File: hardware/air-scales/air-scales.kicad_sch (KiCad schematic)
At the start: 52 parts, among them J1 Connector, USB-TYPE-C-16P, Q1 C458246, SW1 B3FS-1000, SW2 B3FS-1000, U1 BME280, U2 TPS62162DSG, U3 SMA6T28AY, U4 SMA6T15AY, U5 LM74610QDGKTQ1, U6 LM63625DQPWPRQ1, U7 TPS2553DRVR, U8 TPS2121RUXR, U9 ESP32-S3-WROOM-1U-N16R8

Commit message: fixed some schematic bullshit i think, still need tvs on vbus
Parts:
- added C21: 10nF, PCM_JLCPCB:C_0603, symbol PCM_JLCPCB-Capacitors:0603,10nF
- added C22, C23: 100nF, PCM_JLCPCB:C_0603, symbol PCM_JLCPCB-Capacitors:0603,100nF
- added C24, C25, C26: 10uF, PCM_JLCPCB:C_1206, symbol PCM_JLCPCB-Capacitors:1206,10uF
- added D4: ESD5Z5.0, Diode_SMD:D_SOD-523, symbol Diode:ESD5Zxx
- added D5: Red, PCM_JLCPCB:D_0603, symbol PCM_JLCPCB-Diodes:LED,0603,Red
- added D7: YELLOW, PCM_JLCPCB:D_0603, symbol PCM_JLCPCB-Diodes:LED,0603,Red
- added D8: ORANGE, PCM_JLCPCB:D_0603, symbol PCM_JLCPCB-Diodes:LED,0603,Red
- added D9: WS2812B, PCM_JLCPCB:LED-SMD_4P-L1.6-W1.5_XL-1615RGBC-WS2812B, symbol PCM_JLCPCB-Extended:LED, WS2812B, 1615
- added J2, J5: Conn_01x03_Socket, symbol Connector:Conn_01x03_Socket
- added J3: Conn_01x02_Socket, symbol Connector:Conn_01x02_Socket
- added R14, R17, R18: 4.7kΩ, PCM_JLCPCB:R_0603, symbol PCM_JLCPCB-Resistors:0603,4.7kΩ
- added R15, R16: 10kΩ, PCM_JLCPCB:R_0603, symbol PCM_JLCPCB-Resistors:0603,10kΩ
- added R19: 470Ω, PCM_JLCPCB:R_0603, symbol PCM_JLCPCB-Resistors:0603,3.3kΩ
- added R20: 1kΩ, PCM_JLCPCB:R_0603, symbol PCM_JLCPCB-Resistors:0603,3.3kΩ
- C13: Capacitance 120uF -> 10uF; LCSC (none) -> C96446; Price (none) -> 0.021USD; Stock (none) -> 3388297
- C2: Attrition Qty (none) -> 10; Category (none) -> Capacitors,Multilayer Ceramic Capacitors MLCC - SMD/SMT; Class (none) -> Basic Component; LCSC C531423 -> C1546; Manufacturer TDK -> FH(Guangdong Fenghua Advanced Tech); Minimum Qty (none) -> 20; Part CGA2B2C0G2A101JT0Y0F -> 0402CG101J500NT; Price (none) -> 0.004USD; Process (none) -> SMT; Stock (none) -> 2554383; Voltage Rated 100V -> 50V
- C4: LCSC C472849 -> C50254; Price (none) -> 0.032USD; Stock (none) -> 180873
- C5: footprint LM74610:CAP_PC_10X12P7_NCH-M -> CAP_PC_10X12P7_NCH
- C7: Attrition Qty (none) -> 10; LCSC (none) -> C21120; Minimum Qty (none) -> 20; Part (none) -> CL10B224KA8NNNC; Stock (none) -> 781839; Voltage Rated 50V -> 25V
- D1, D2: Attrition Qty (none) -> 4; LCSC C20345394 -> C42413899; Manufacturer TI -> hongjiacheng; Minimum Qty (none) -> 5; Part ESD321DYAR -> H5VND5BA; Price (none) -> 0.032USD; Stock (none) -> 10812
- D3: Attrition Qty (none) -> 4; Class (none) -> Preferred Component; LCSC C22427765 -> C41411782; Manufacturer TI -> hongjiacheng; Minimum Qty (none) -> 15; Part ESD441DPLR -> SMF20A; Price (none) -> 0.026USD; Process (none) -> SMT; Stock (none) -> 34292
- D6: value Red -> GREEN
- L1: footprint Inductor_SMD:L_Coilcraft_1515SQ-68N -> PCM_JLCPCB:L_0805; Attrition Qty (none) -> 10; Class (none) -> Preferred Component; Frequency - Self Resonant (none) -> 50MHz; LCSC C404494 -> C1043; Manufacturer TDK -> FH(Guangdong Fenghua Advanced Tech); Minimum Qty (none) -> 20; Part VLS3012HBX-2R2M -> CMI201209U2R2KT; Price (none) -> 0.011USD; Process SMD -> SMT; Q @ Freq (none) -> 35@10MHz; Stock (none) -> 114084
- R3: value 3.3kΩ -> 1kΩ; Attrition Qty 10 -> (none); LCSC C22978 -> (none); Minimum Qty 20 -> (none); Price 0.004USD -> (none); Process SMT -> (none); Resistance 3.3kΩ -> 1kΩ; Stock 2152628 -> (none)
- U3, U4: footprint SMA6T28AY:SMA_UNI_STM -> SMA_UNI_STM
- U5: footprint LM74610:DGK0008A_N -> LM74610QDGKTQ1:SOP65P490X110-8N
- U9: footprint ESP32:XCVR_ESP32-S3-WROOM-1U-N16R8 -> ESP32-S3-WROOM-1U-N16R8:XCVR_ESP32-S3-WROOM-1U-N16R8
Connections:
- net +5V MAIN is gone; now on net +5V VEHICLE: C10.1, L2.2, U6.9 (FB), U8.6 (PR1), U8.7 (IN1)
- net -BATT is gone; now on net -12V BATT: C1.2, C11.2, C12.2, C13.2, C14.2, C15.2, C16.2, C17.2, C18.2, C19.2, C2.2, C20.2, C3.2, C5.2, C6.2, C7.2, C8.2, D1.1, D2.1, D3.1, D6.1, J1.A12B1 (GND), J1.B12A1 (GND), J1.S1 (SHIELD), R1.2, R2.2, R4.2, R8.2, R9.2, SW1.3, SW1.4, SW2.3, SW2.4, U1.1 (GND), U1.7 (GND), U2.1 (PGND), U2.4 (AGND), U2.5 (FB), U4.2 (A), U6.10 (AGND), U6.15 (PGND), U6.16 (PGND), U6.17 (PAD), U6.5 (RT), U6.7 (SYNC_MODE), U7.5 (GND), U8.12 (GND), U8.4 (OV2), U8.5 (OV1), U9.1 (GND), U9.40 (GND__1), U9.41_1 (GND__2), U9.41_2 (GND__3), U9.41_3 (GND__4), U9.41_4 (GND__5), U9.41_5 (GND__6), U9.41_6 (GND__7), U9.41_7 (GND__8), U9.41_8 (GND__9), U9.41_9 (GND__10)
- net +3.3V: now also U1.2 (CSB), U1.6 (VDDIO), U1.8 (VDD), C23.1, C24.1, D9.2 (VDD), R17.1, R18.1, R19.1
- net +5V USB: now also C26.1, R20.1
- net SCL: now also R18.2
- net SDA: now also R17.2
- net U0RXD: now also J5.3 (Pin_3)
- net U0TXD: now also J5.2 (Pin_2)
- net at C5.1, C6.1, C7.1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: no longer U5.8 (CATHODE)
- net +5V VEHICLE: now reaches C11.1
- net +5V VEHICLE: now also C25.1; no longer C10.2
- net at U5.1 (VCAPL): no longer C4.2
- net at U5.7 (VCAPH): no longer C4.1
- net -12V BATT: now reaches U1.5 (SDO)
- net -12V BATT: now also C10.2, C21.2, C22.2, C23.2, C24.2, C25.2, C26.2, D4.1 (K), D5.1, D7.1, D8.1, D9.3 (GND), J2.1 (Pin_1), J3.2 (Pin_2), J5.1 (Pin_1), R15.2
- net PRESSURE_IN: now reaches U9.4 (IO4)
- net PRESSURE_IN: now also C21.1, C22.1, R14.2, R15.1
- net LED: now reaches U9.5 (IO5)
- net LED: now also D9.4 (DIN)
- net +5V SYS renamed +5V_SYS
- net +5V_SYS: now also J2.2 (Pin_2)
- net +BATT renamed +12V BATT
- net +12V BATT: now also J3.1 (Pin_1), R16.1; no longer U5.4 (ANODE)
- net VBUS: no longer names the net of C12.1, J1.A9B4 (VBUS), J1.B9A4 (VBUS), R7.1, U7.6 (IN)
- new net: D7.2, R19.2
- new net: D5.2, R16.2
- new net: D8.2, R20.2
- new net PX2_IN: D4.2 (A), J2.3 (Pin_3), R14.1
- now unconnected: Q1.4 (G), U5.2 (GATE_PULL_DOWN), U5.6 (GATE_DRIVE)
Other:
- note added: "0x76 IS THE ADDRESS FOR THE I2C ON THE BME280"
- note added: "AMBIENT PRESSURE AND TEMP SENSOR"
- note added: "Arbitrating 5 V rails"
- note added: "BOOT AND RESET BUTTONS"
- note added: "EXTERNAL FEMALE CONNECTORS"
- note added: "MAIN MICROCONTROLLER"
- note added: "SIGNAL CONDITIONING ON PX2AF1XX150PSAAX LINE"
- note added: "SYS POWER (5V) TO 3.3V"
- note added: "USB POWER TO 5V"
- note added: "Vehicle Battery to 5V"
- note removed: "Bullshit on ESD and Surge Protection for USB Interfaces by Texas Instruments"
- note removed: "TVS (12 V line): SMBJ36A (600 W). Ideal diode (12 V): LM74610-Q1 + 40 V, 10-20 mΩ N-MOSFET (SO-8 PowerPAK-ish). Buck (12 V→5 V): LM63625-Q1; L = 3.3-4.7 µH ≥3 A; Cout = 2×22 µF/10 V. USB switch: TPS2553 (or any 5 V eFuse 0.5-1 A). Dual ORing (to SYS_5V): LM66100 ×2 (one on each 5 V path). Buck (5 V→3.3 V): TPS62840-Q1 (or TPS62162-Q1); L ≈2.2 µH; Cout ≈22-30 µF. Sensor 5 V filter: 10 µH + 10 µF/1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"
- company: AirScales -> Air Scales
- moved on the sheet: C1, C10, C11, C12, C13, C14, C15, C16, C17, C18, C19, C2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

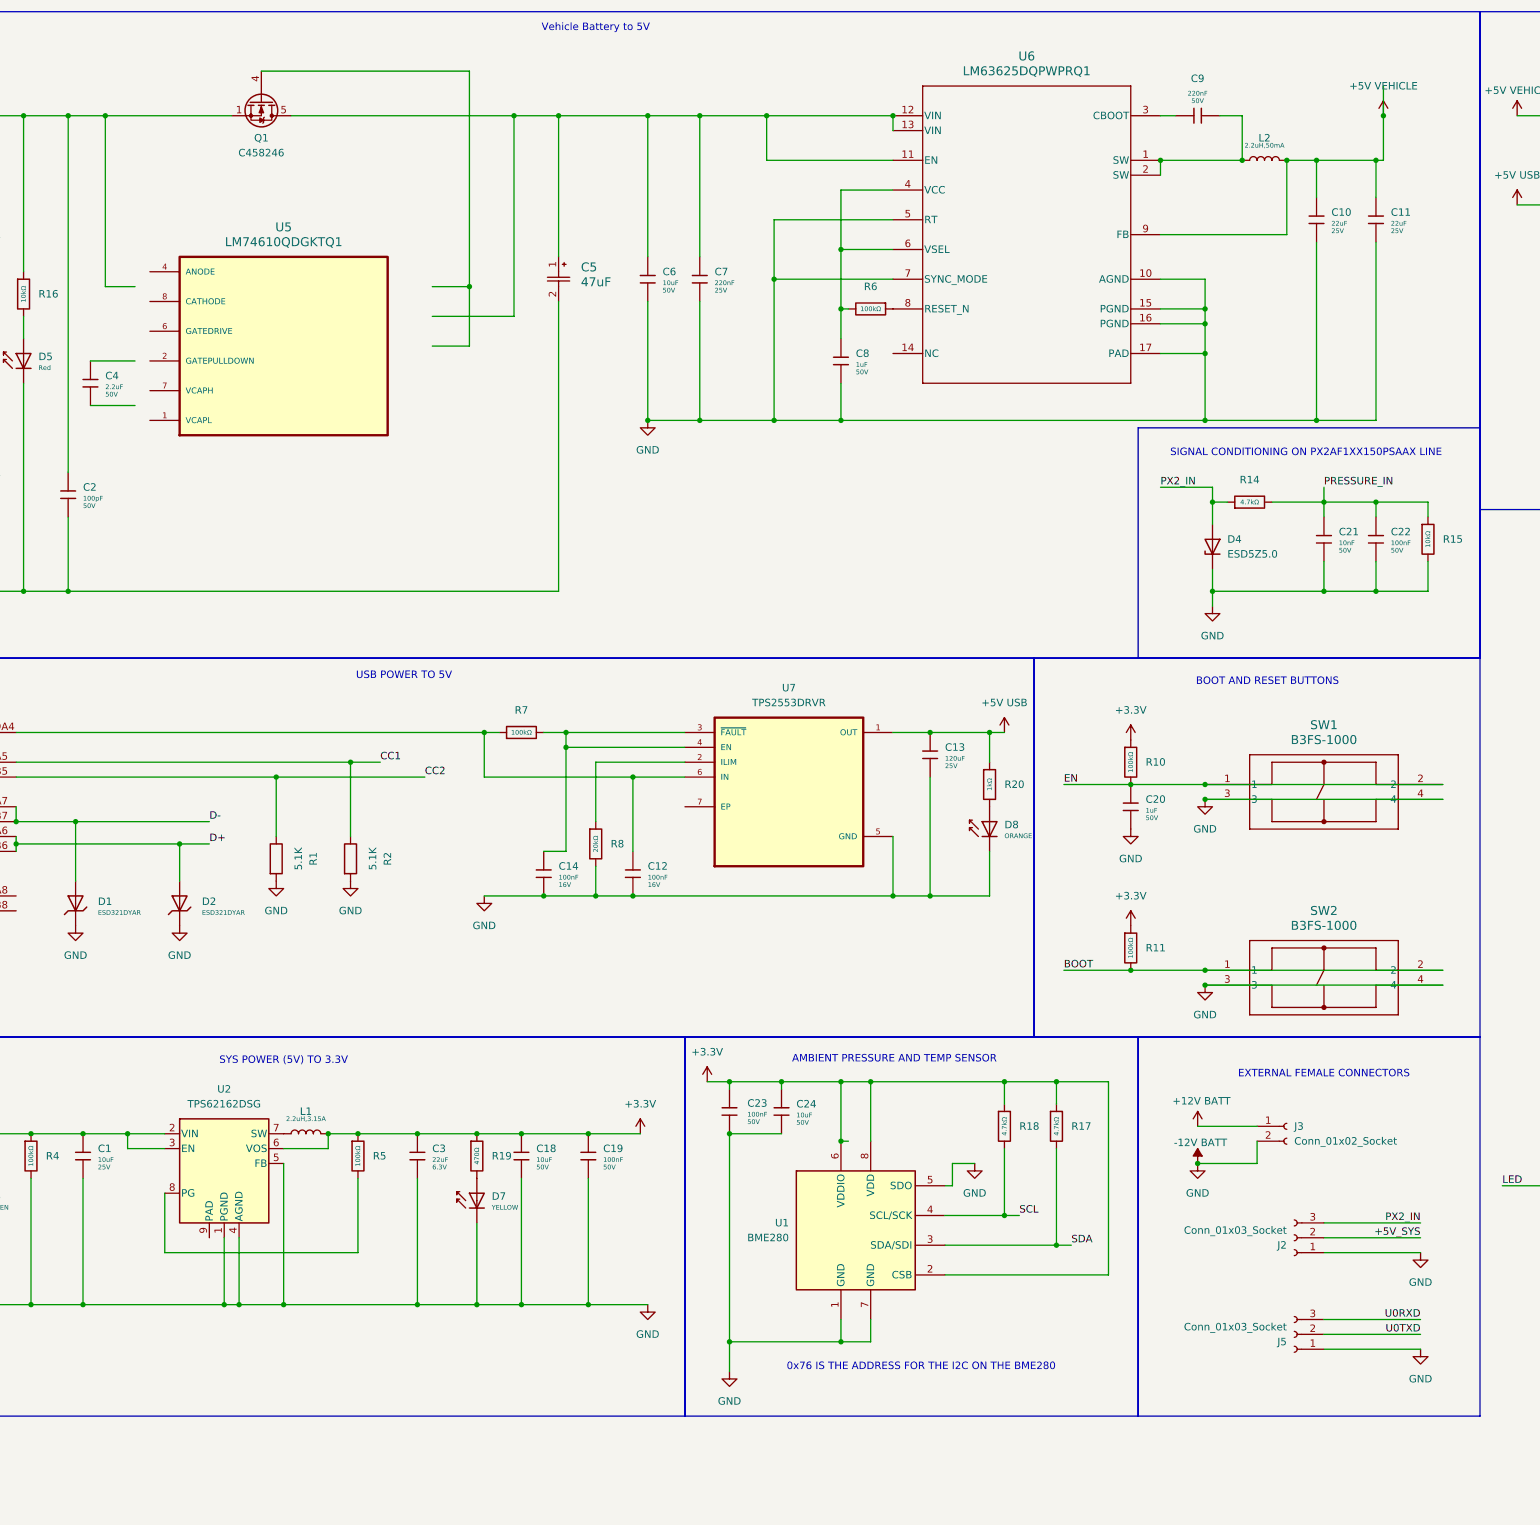
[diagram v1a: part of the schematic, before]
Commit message: updated all the footprints.pretty i think
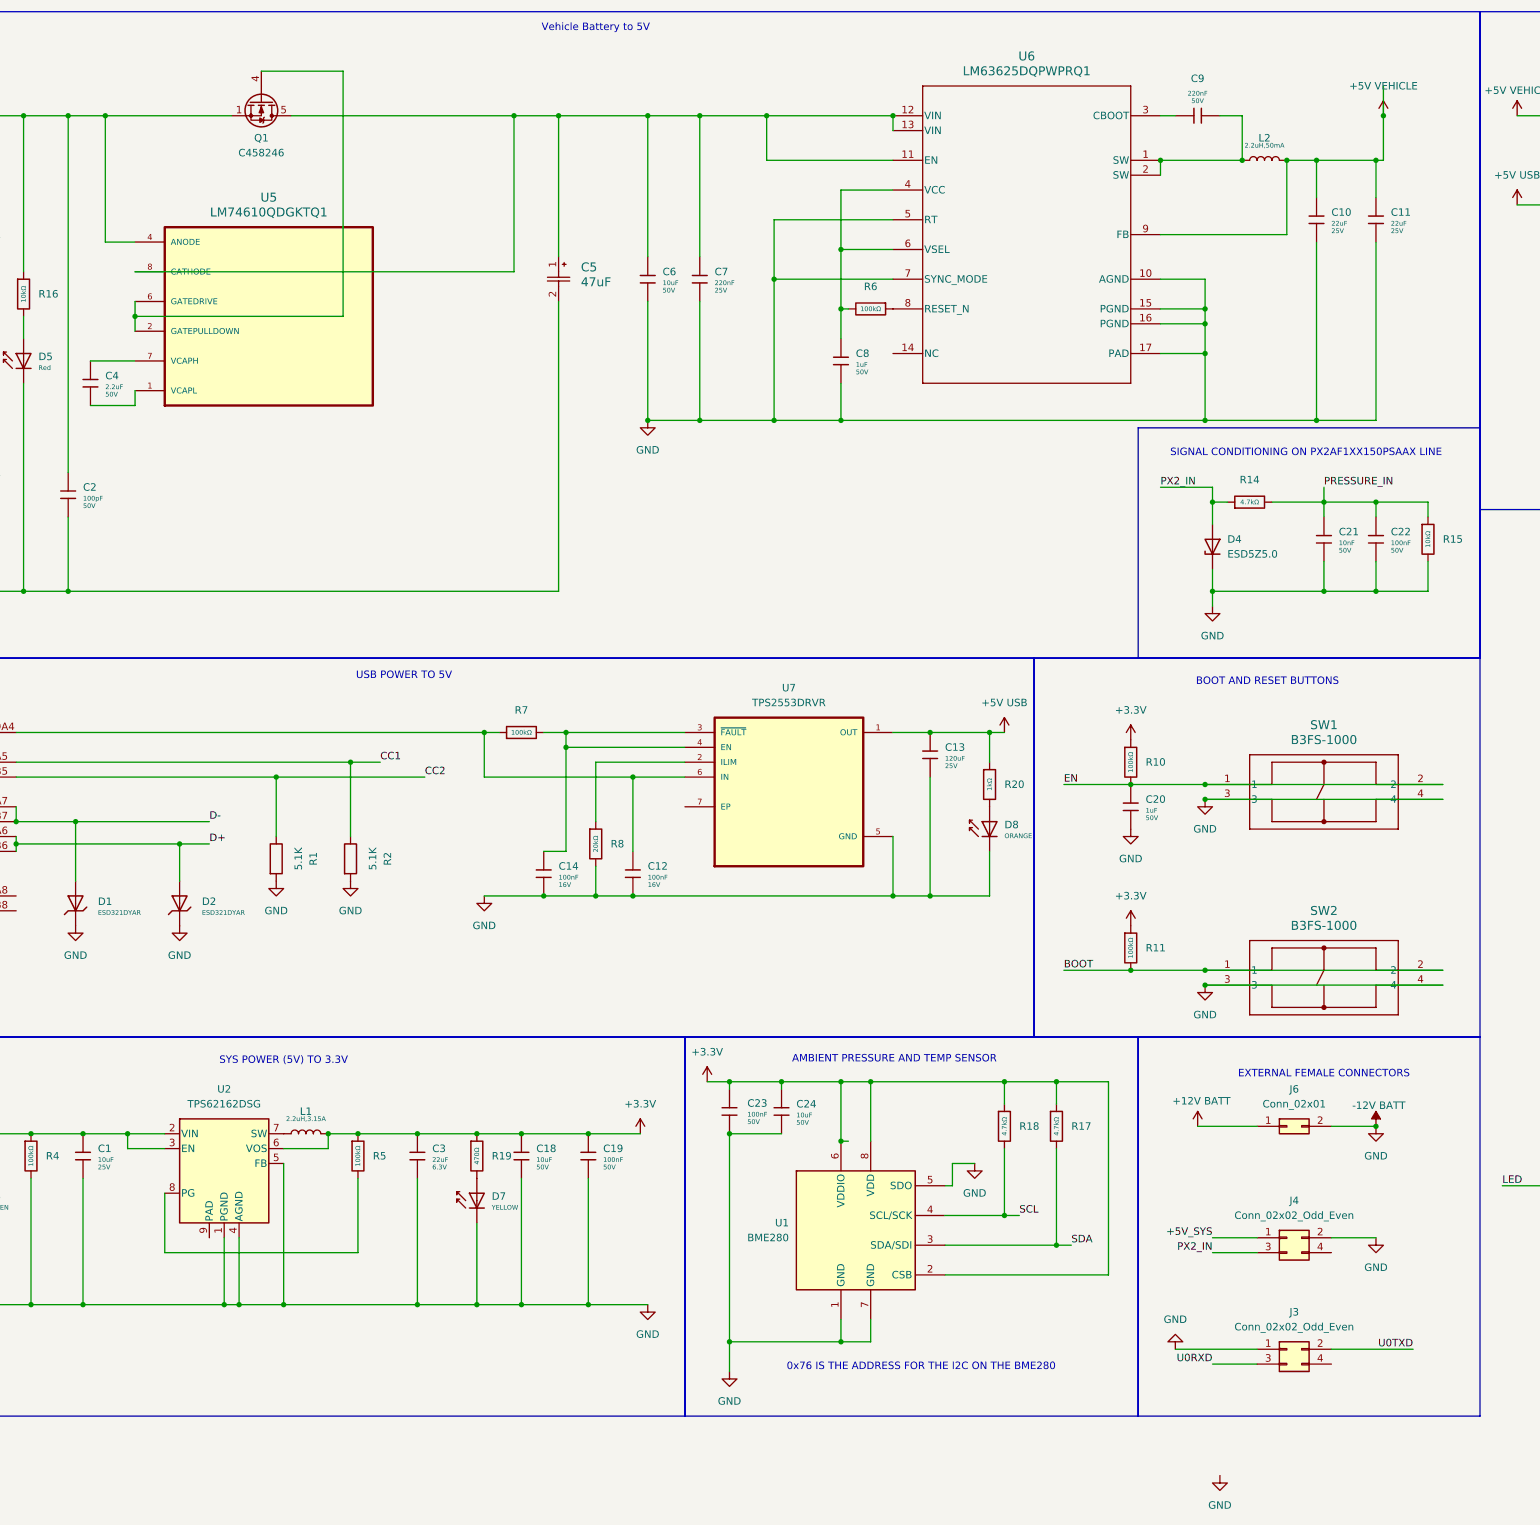
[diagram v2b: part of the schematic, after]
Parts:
- removed J2, J5: Conn_01x03_Socket, symbol Connector:Conn_01x03_Socket
- removed J3: Conn_01x02_Socket, symbol Connector:Conn_01x02_Socket
- added J3, J4: Conn_02x02_Odd_Even, Connector_Molex:Molex_Micro-Fit_3.0_43045-0418_2x02-1MP_P3.00mm_Vertical, symbol Connector_Generic:Conn_02x02_Odd_Even
- added J6: Conn_02x01, Connector_Molex:Molex_Micro-Fit_3.0_43045-0218_2x01-1MP_P3.00mm_Vertical, symbol Connector_Generic:Conn_02x01
- C5: footprint CAP_PC_10X12P7_NCH -> 10X12P7_NCH:CAP_PC_10X12P7_NCH
- SW1, SW2: footprint SW_B3FS-1000_OMR -> B3FS-1000:SW_B3FS-1000_OMR
- U3, U4: footprint SMA_UNI_STM -> SMA6T28AY:SMA_UNI_STM
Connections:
- net +12V BATT: now also U5.4 (ANODE), J6.1 (Pin_1)
- net +5V_SYS: now also J4.1 (Pin_1)
- net -12V BATT: now also J3.1 (Pin_1), J4.2 (Pin_2), J6.2 (Pin_2)
- net PX2_IN: now also J4.3 (Pin_3)
- net U0RXD: now also J3.3 (Pin_3)
- net U0TXD: now also J3.2 (Pin_2)
- net at C5.1, C6.1, C7.1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: now also U5.8 (CATHODE)
- net at U5.1 (VCAPL): now also C4.2
- net at U5.2 (GATEPULLDOWN): now also Q1.4 (G), U5.6 (GATEDRIVE)
- net at U5.7 (VCAPH): now also C4.1
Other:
- moved on the sheet: U5

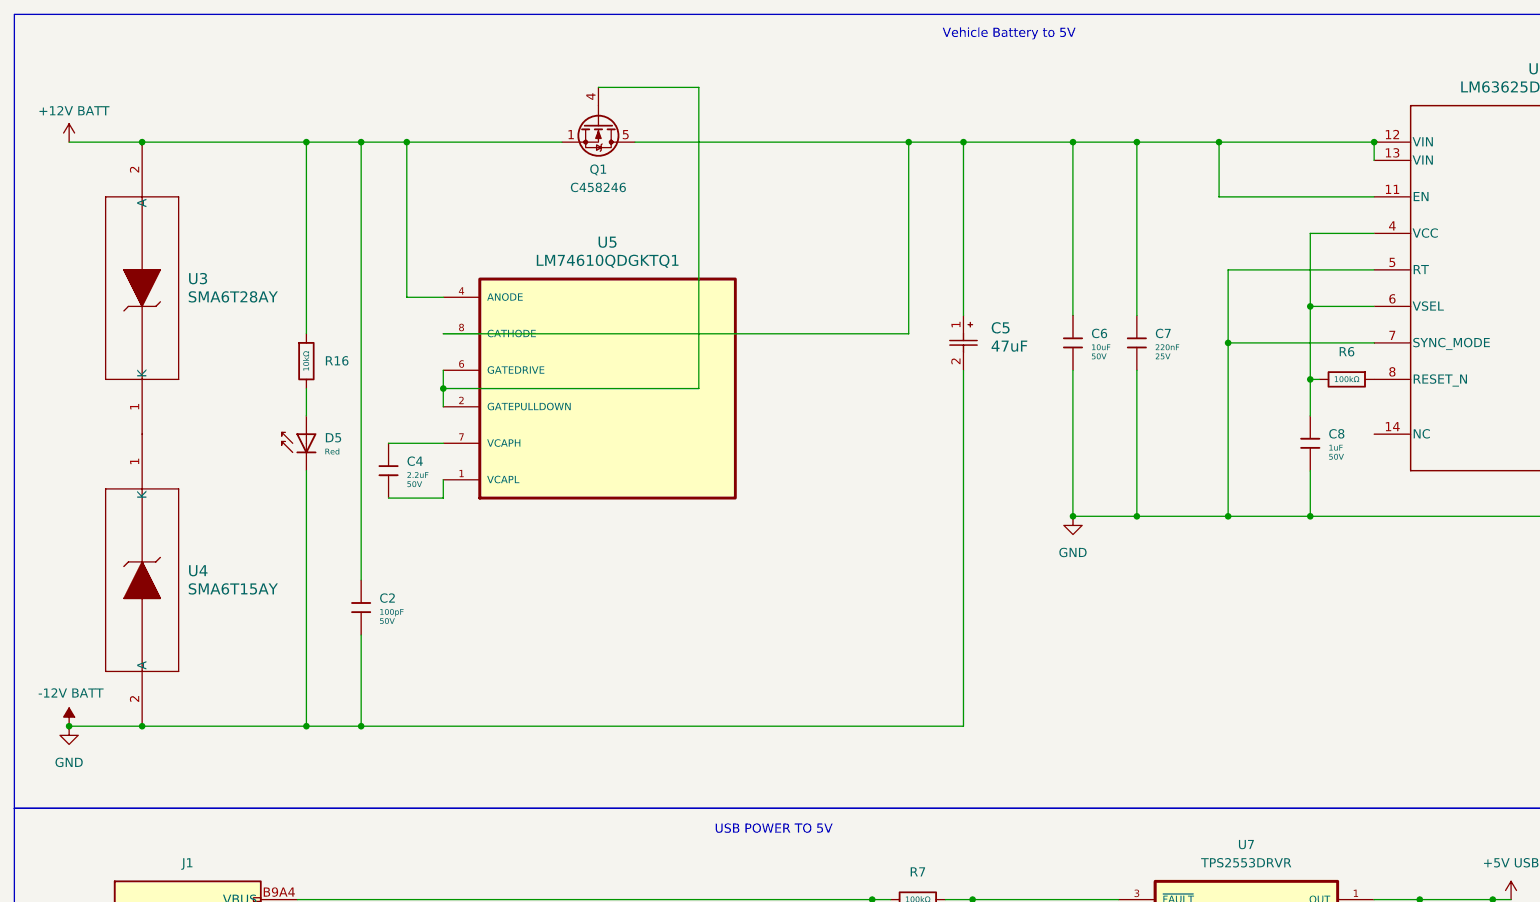
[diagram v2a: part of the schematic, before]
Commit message: tvs was wrong before lm74610 so fixed that
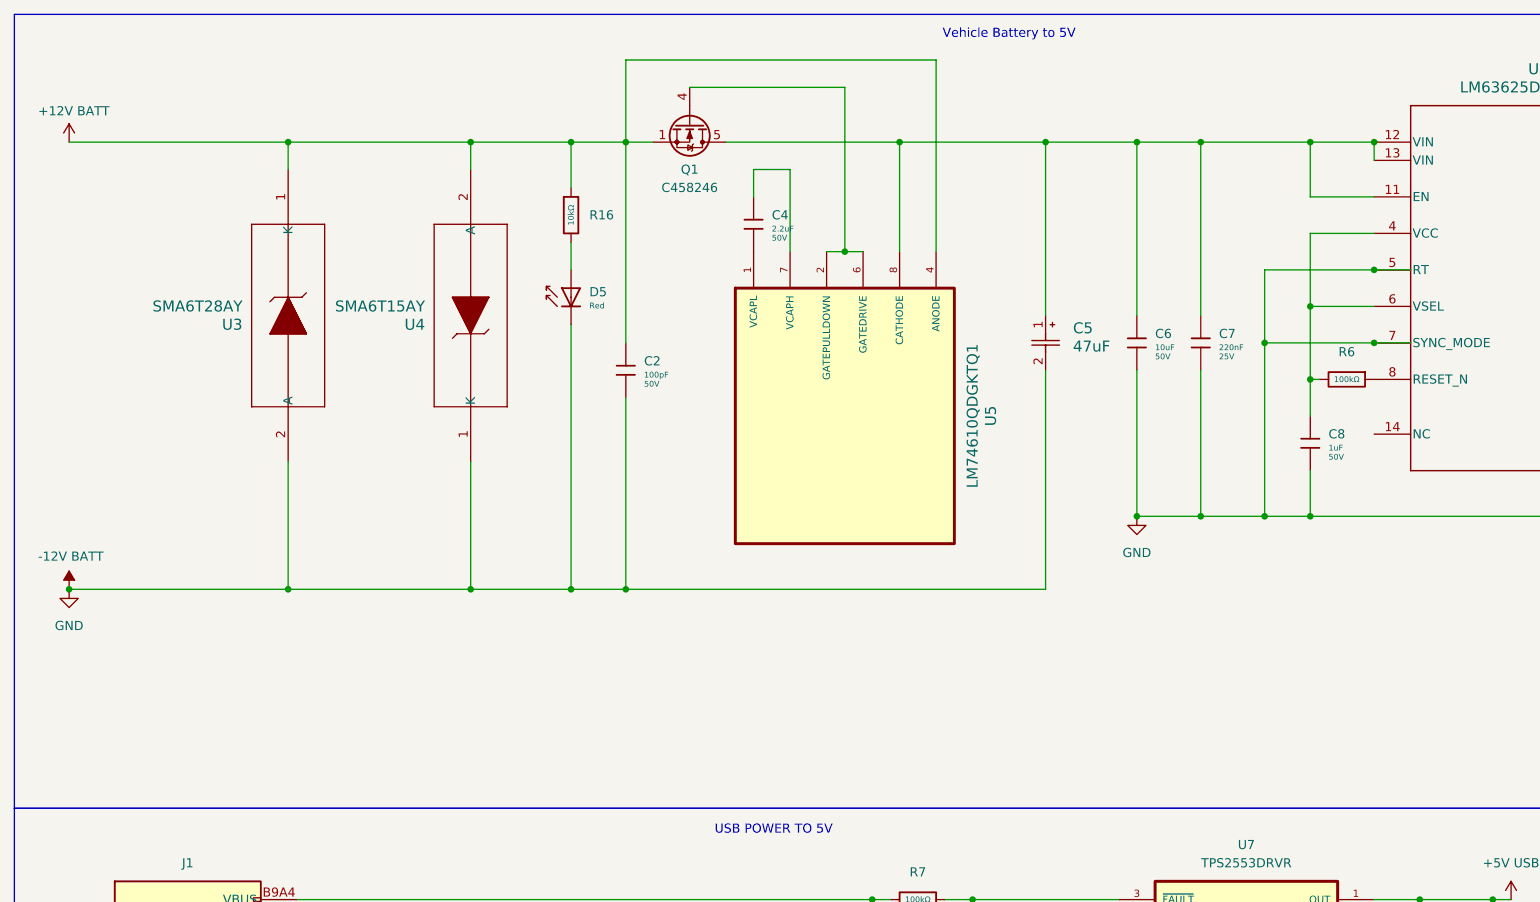
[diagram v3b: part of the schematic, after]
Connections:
- net +12V BATT: now also U3.1 (K), U4.2 (A); no longer U3.2 (A)
- net -12V BATT: now also U3.2 (A), U4.1 (K); no longer U4.2 (A)
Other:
- moved on the sheet: C2, C4, C5, C6, C7, D5, Q1, R16, U3, U4, U5
